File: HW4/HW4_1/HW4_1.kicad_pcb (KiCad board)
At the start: 2 copper layers, 50 x 50 mm, 23 parts, among them J1 CP2102N, J2 Battery, J3 Conn_01x12_Pin, J4 Conn_01x12_Pin, SW1 RESET, SW2 USER, SW3 SW_DPDT_x2, U1 PIC32MX170F256B, U2 AP7381-33Y

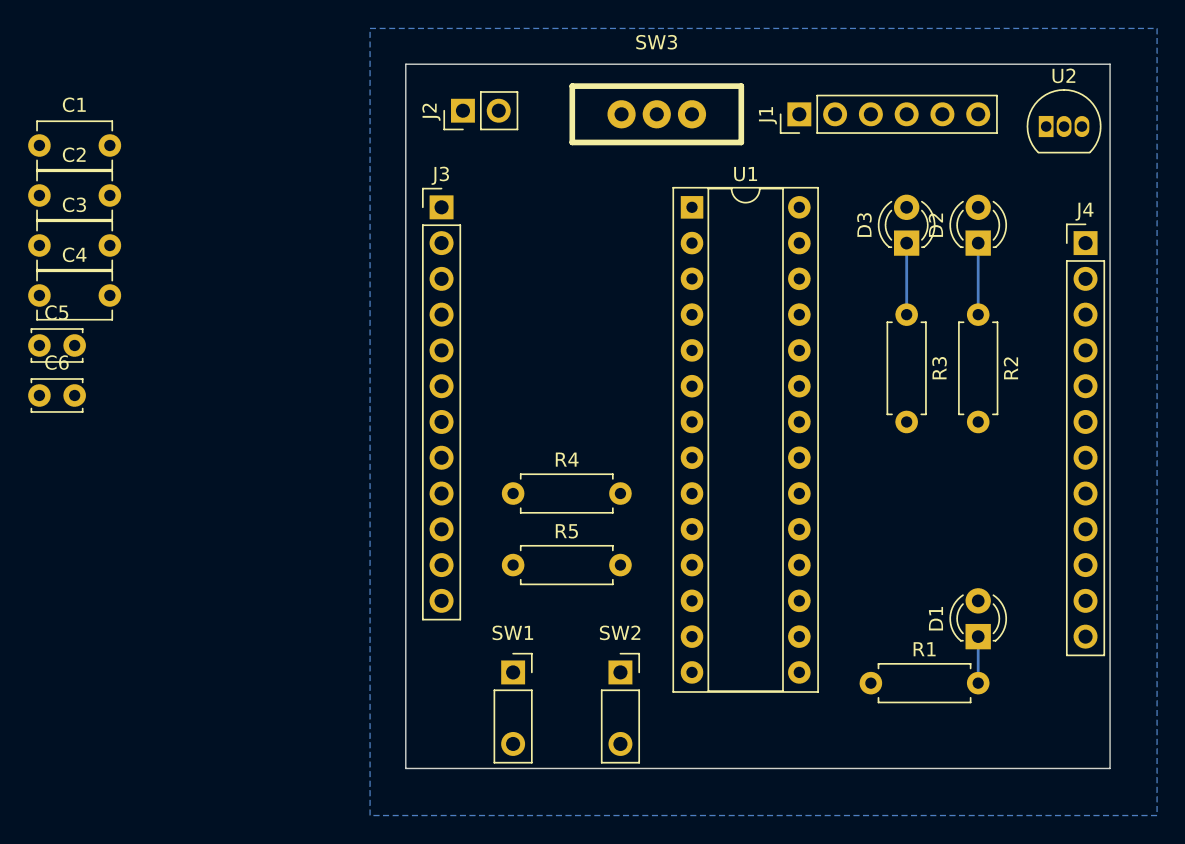
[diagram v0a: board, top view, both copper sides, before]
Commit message: board start routing
Bug to resolve: Pushbuttons have both pins GND, but assigned correctly in schematic
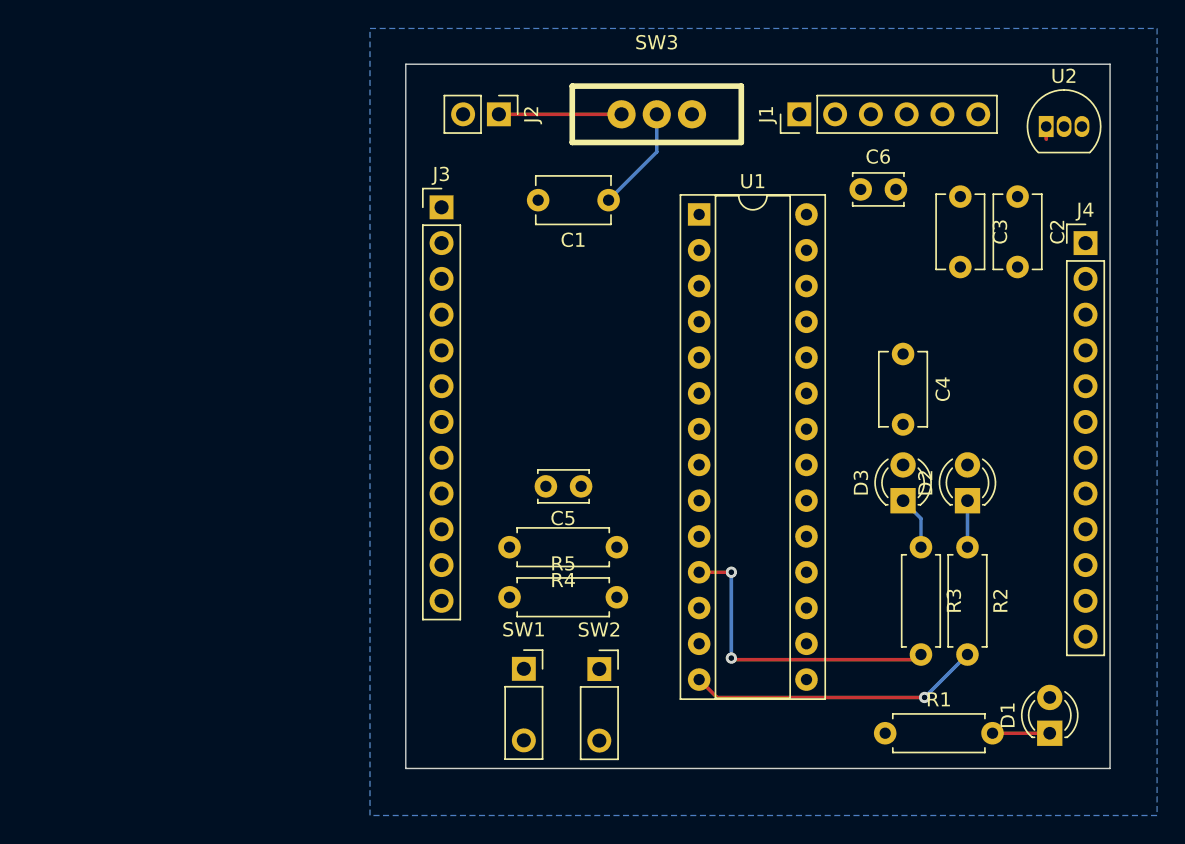
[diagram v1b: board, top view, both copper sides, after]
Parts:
- moved C2 69.4 mm to (170.4, 60.2), turned to -90 degrees
- moved C3 65.5 mm to (166.4, 60.2), turned to -90 degrees
- moved C4 61.5 mm to (162.3, 71.4), turned to -90 degrees
- moved C6 60.1 mm to (159.3, 59.7)
- moved C1 40.6 mm to (141.4, 60.5), turned to 180 degrees
- moved C5 39.7 mm to (139.4, 80.8), turned to 180 degrees
- moved D2 18.3 mm to (166.9, 81.8)
- moved D3 18.3 mm to (162.3, 81.8)
- moved R3 16.5 mm to (163.6, 85.1)
- moved R2 16.5 mm to (166.9, 85.1)
- moved D1 8.53 mm to (172.7, 98.3)
- moved R4 8.29 mm to (142.0, 85.1), turned to 180 degrees
- moved R1 3.70 mm to (161.0, 98.3)
- moved J2 2.56 mm to (133.6, 54.4), turned to -90 degrees
- moved R5 2.30 mm to (134.4, 88.6)
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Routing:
- net /GREEN: track 0.00 -> 22.0 mm, vias 0 -> 2
- net /YELLOW: track 0.00 -> 20.8 mm, vias 0 -> 1
- net Net-(J2-Pin_1): track 0.00 -> 8.71 mm
- net /Vin: track 0.00 -> 7.51 mm
- net Net-(D1-K): track 0.00 -> 4.06 mm
- net Net-(D3-K): track 0.00 -> 3.83 mm
- net Net-(D2-K): track 0.00 -> 3.30 mm
- net +3.3V: track 0.00 -> 0.91 mm

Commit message: implemented I2C HW6
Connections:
- SW1 pad 1: GND -> /MCLR
- SW2 pad 1: GND -> /A4
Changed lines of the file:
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@@
       (stroke (width 0.1) (type solid)) (layer "F.Fab"))
     (pad "1" thru_hole rect (at 0 0) (size 1.7 1.7) (drill 1) (layers "*.Cu" "*.Mask")
-      (net 2 "GND") (pinfunction "A") (pintype "passive"))
+      (net 32 "/MCLR") (pinfunction "A") (pintype "passive"))
     (pad "2" thru_hole oval (at 0 5.08) (size 1.7 1.7) (drill 1) (layers "*.Cu" "*.Mask")
       (net 2 "GND") (pinfunction "A") (pintype "passive"))
@@
       (stroke (width 0.1) (type solid)) (layer "F.Fab"))
     (pad "1" thru_hole rect (at 0 0) (size 1.7 1.7) (drill 1) (layers "*.Cu" "*.Mask")
-      (net 2 "GND") (pinfunction "A") (pintype "passive"))
+      (net 33 "/A4") (pinfunction "A") (pintype "passive"))
     (pad "2" thru_hole oval (at 0 5.08) (size 1.7 1.7) (drill 1) (layers "*.Cu" "*.Mask")
       (net 2 "GND") (pinfunction "A") (pintype "passive"))

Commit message: PCB finished
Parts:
- moved R4 7.62 mm to (134.4, 85.1), turned to 0 degrees
- moved J3 3.14 mm to (128.8, 64.0)
- moved C5 2.52 mm to (136.9, 80.8), turned to 0 degrees
- moved J4 0.51 mm to (175.3, 64.0)
- renumbered J1 to CP2102
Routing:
- net +3.3V: track 0.91 -> 113.1 mm, vias 0 -> 8
- net /Vin: track 7.51 -> 115.5 mm, vias 0 -> 4
- net /MCLR: track 0.00 -> 45.2 mm, vias 0 -> 1
- net /B6: track 0.00 -> 35.7 mm, vias 0 -> 2
- net /YELLOW: track 20.8 -> 55.6 mm, vias 1 -> 3
- net /U1TX: track 0.00 -> 31.4 mm
- net /U1RX: track 0.00 -> 28.7 mm, vias 0 -> 1
- net /SCL1-B8: track 0.00 -> 27.3 mm, vias 0 -> 2
- net /B7: track 0.00 -> 26.9 mm, vias 0 -> 2
- net /SDA1-B9: track 0.00 -> 25.9 mm, vias 0 -> 2
- net /A3: track 0.00 -> 22.2 mm
- net /GREEN: track 22.0 -> 44.2 mm
- net /SCK2-B15: track 0.00 -> 20.9 mm
- net /B13: track 0.00 -> 20.9 mm
- net /B12: track 0.00 -> 20.9 mm
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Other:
- board text added: "3V3"
- board text added: "A0"
- board text added: "A1"
- board text added: "A3"
- board text added: "B0"
- board text added: "B1"
- board text added: "B10"
- board text added: "B11"
- board text added: "B12"
- board text added: "B13"
- board text added: "B14"
- board text added: "B15"
- board text added: "B2"
- board text added: "B4"
- board text added: "B5"
- board text added: "B6"
- board text added: "B7"
- board text added: "B8"
- board text added: "B9"
- board text added: "GND"
- board text added: "VIN"
